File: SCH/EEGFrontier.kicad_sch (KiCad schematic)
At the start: 29 parts, among them J1 Conn_01x08_Pin, SW1 SW_Push, U1 102010428, U2 ADS1299-4PAGR

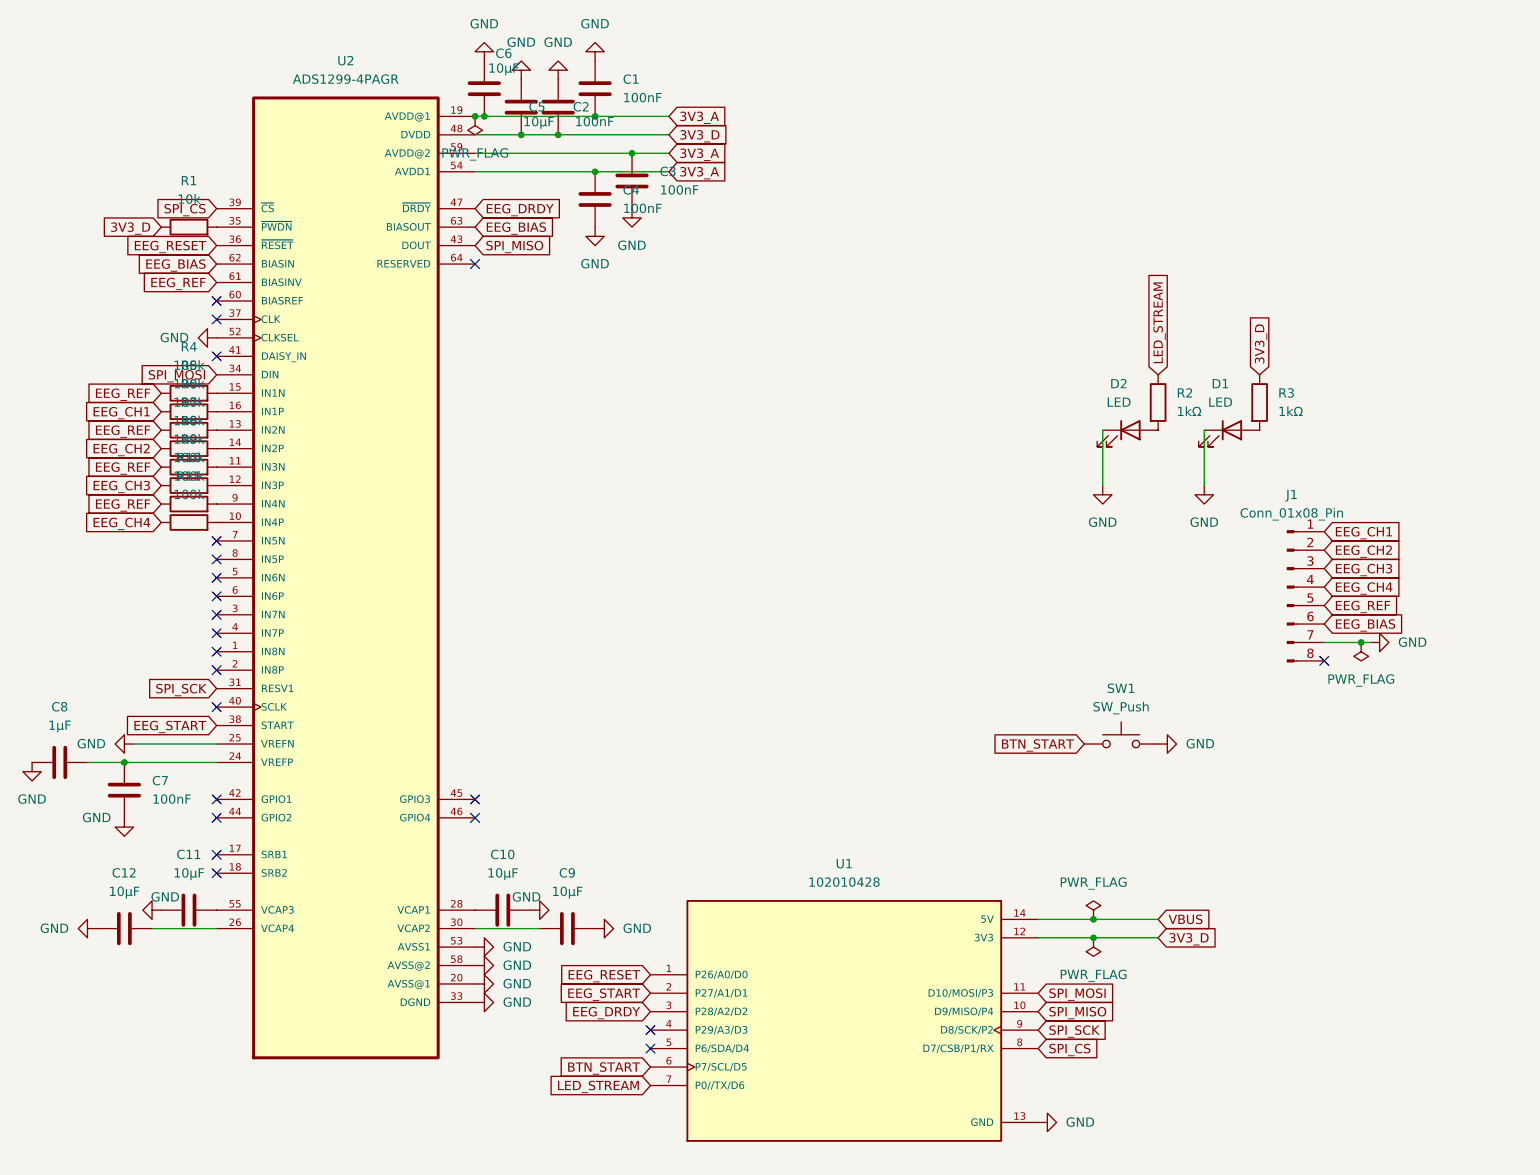
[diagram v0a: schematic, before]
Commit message: feat(hw): launch EEGFrontier V2 with ADS1299IPAGR and 8-channel PCB update
- migrate analog front-end from ADS1299-4PAGR (V1) to ADS1299IPAGR (V2)
- expand hardware target from 4 EEG channels to 8 channels
- apply PCB noise-reduction rework:
  - reduce direct GND trace routing in sensitive analog areas
  - adopt curved track routing for cleaner analog paths
- update KiCad design artifacts (PCB/SCH) and generated fabrication outputs
- add V2 hardware assets (3D front/back, PCB view)
- refresh README with V1 vs V2 comparisons and updated project status

TODO (next steps):
- update BOM for V2 components and pricing
- update/validate firmware for V2 hardware revision

Refs #4
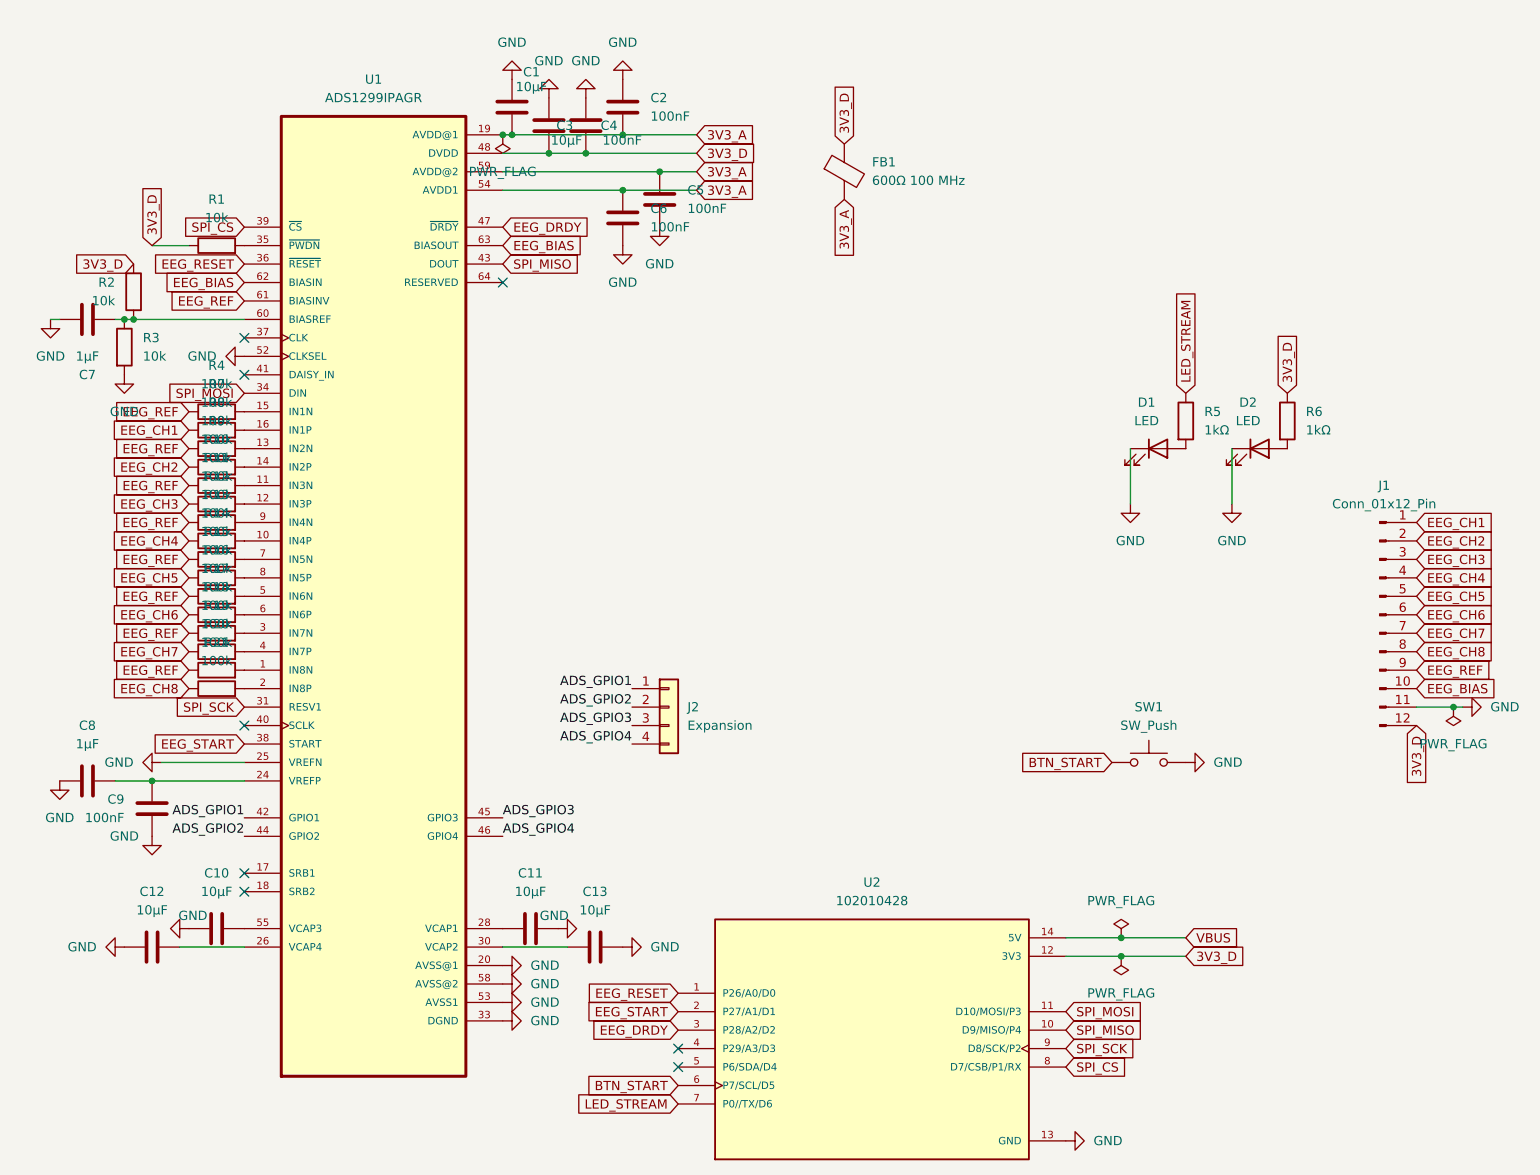
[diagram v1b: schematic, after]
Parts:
- removed J1: Conn_01x08_Pin, Connector_PinHeader_2.54mm:PinHeader_1x08_P2.54mm_Horizontal, symbol Connector:Conn_01x08_Pin
- removed U2: ADS1299-4PAGR, OPL:QFP50P1200X1200X120-64N, symbol ADS1299-4PAGR:ADS1299-4PAGR
- added C7: 1µF, Capacitor_SMD:C_0603_1608Metric, symbol Device:C
- added FB1: 600Ω 100 MHz, Resistor_SMD:R_0805_2012Metric, symbol Device:FerriteBead
- added J1: Conn_01x12_Pin, Connector_PinHeader_2.54mm:PinHeader_1x12_P2.54mm_Horizontal, symbol Connector:Conn_01x12_Pin
- added J2: Expansion, Connector_PinHeader_2.54mm:PinHeader_1x04_P2.54mm_Horizontal, symbol Connector_Generic:Conn_01x04
- added R14, R15, R16, R17, R18, R19, R20, R21: 100k, Resistor_SMD:R_0805_2012Metric, symbol Device:R
- added R2, R3: 10k, Resistor_SMD:R_0805_2012Metric, symbol Device:R
- added U1: ADS1299IPAGR, OPL:QFP50P1200X1200X120-64N, symbol ADS1299IPAGR:ADS1299IPAGR
- renumbered C6 to C1, C11 to C10, C10 to C11, C9 to C13, C1 to C2, C5 to C3, C2 to C4, C3 to C5, C4 to C6, C7 to C9, D2 to D1, D1 to D2, R8 to R10, R9 to R11, R10 to R12, R11 to R13, R2 to R5, R3 to R6, R5 to R7, R6 to R8, R7 to R9, U1 to U2
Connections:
- net AVDD@1: now also FB1.2, U1.19 (AVDD@1), U1.21 (AVDD@1), U1.22 (AVDD@1), U1.54 (AVDD1), U1.56 (AVDD@1), U1.59 (AVDD@2)
- net AVSS@1: now also C7.2, J1.11 (Pin_11), R3.2, U1.20 (AVSS@1), U1.23 (AVSS@1), U1.25 (VREFN), U1.32 (AVSS@1), U1.33 (DGND), U1.49 (DGND), U1.51 (DGND), U1.52 (CLKSEL), U1.53 (AVSS1), U1.57 (AVSS@1), U1.58 (AVSS@2)
- net DVDD: now also FB1.1, J1.12 (Pin_12), R2.2, U1.48 (DVDD), U1.50 (DVDD)
- net EEG_BIAS: now also J1.10 (Pin_10), U1.62 (BIASIN), U1.63 (BIASOUT)
- net EEG_CH1: now also J1.1 (Pin_1)
- net EEG_CH2: now also J1.2 (Pin_2)
- net EEG_CH3: now also J1.3 (Pin_3)
- net EEG_CH4: now also J1.4 (Pin_4)
- net EEG_DRDY: now also U1.47 (~{DRDY})
- net EEG_REF: now also J1.9 (Pin_9), R14.1, R16.1, R18.1, R20.1, U1.61 (BIASINV)
- net EEG_RESET: now also U1.36 (~{RESET})
- net EEG_START: now also U1.38 (START)
- net SPI_CS: now also U1.39 (~{CS})
- net SPI_MISO: now also U1.43 (DOUT)
- net SPI_MOSI: now also U1.34 (DIN)
- net SPI_SCK: now also U1.31 (RESV1)
- net at R8.2: now also U1.13 (IN2N)
- net at C13.1: now also U1.30 (VCAP2)
- net at R1.2: now also U1.35 (~{PWDN})
- net at R11.2: now also U1.12 (IN3P)
- net at C10.1: now also U1.55 (VCAP3)
- net at C12.1: now also U1.26 (VCAP4)
- net at R12.2: now also U1.9 (IN4N)
- net at R7.2: now also U1.16 (IN1P)
- net at C8.1, C9.1: now also U1.24 (VREFP)
- net at R9.2: now also U1.14 (IN2P)
- net at C11.1: now also U1.28 (VCAP1)
- net at R13.2: now also U1.10 (IN4P)
- net at R10.2: now also U1.11 (IN3N)
- net at R4.2: now also U1.15 (IN1N)
- new net: C7.1, R2.1, R3.1, U1.60 (BIASREF)
- new net: R20.2, U1.1 (IN8N)
- new net: R17.2, U1.6 (IN6P)
- new net: R21.2, U1.2 (IN8P)
- new net: R18.2, U1.3 (IN7N)
- new net: R19.2, U1.4 (IN7P)
- new net: R16.2, U1.5 (IN6N)
- new net: R14.2, U1.7 (IN5N)
- new net: R15.2, U1.8 (IN5P)
- new net ADS_GPIO1: J2.1 (Pin_1), U1.42 (GPIO1)
- new net ADS_GPIO2: J2.2 (Pin_2), U1.44 (GPIO2)
- new net ADS_GPIO3: J2.3 (Pin_3), U1.45 (GPIO3)
- new net ADS_GPIO4: J2.4 (Pin_4), U1.46 (GPIO4)
- new net EEG_CH5: J1.5 (Pin_5), R15.1
- new net EEG_CH6: J1.6 (Pin_6), R17.1
- new net EEG_CH7: J1.7 (Pin_7), R19.1
- new net EEG_CH8: J1.8 (Pin_8), R21.1
- no-connect marks 22 -> 8
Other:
- moved on the sheet: C1, C10, C11, C12, C13, C2, C3, C4, C5, C6, C8, C9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
